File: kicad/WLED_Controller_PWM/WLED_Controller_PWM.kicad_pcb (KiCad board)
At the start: 2 copper layers, 72 x 50 mm, 59 parts, among them J1 USB_C_Receptacle_USB2.0, J5 Conn_01x05, J6 Conn_01x02, Q1 BC847, Q2 BC847, Q3 IRFL4105PBF, Q4 IRFL4105PBF, Q5 IRFL4105PBF, Q6 IRFL4105PBF, SW1 SW_RESET, SW2 SW_BOOT, SW3 SW_Push, U1 ESP32-WROOM-32, U2 CH340C, U3 NCP1117-3.3, U4 TSSP58P38, U5 L7805

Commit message: change mosfet
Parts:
- Q3, Q4, Q5, Q6: value IRFL4105PBF -> IRLL2705

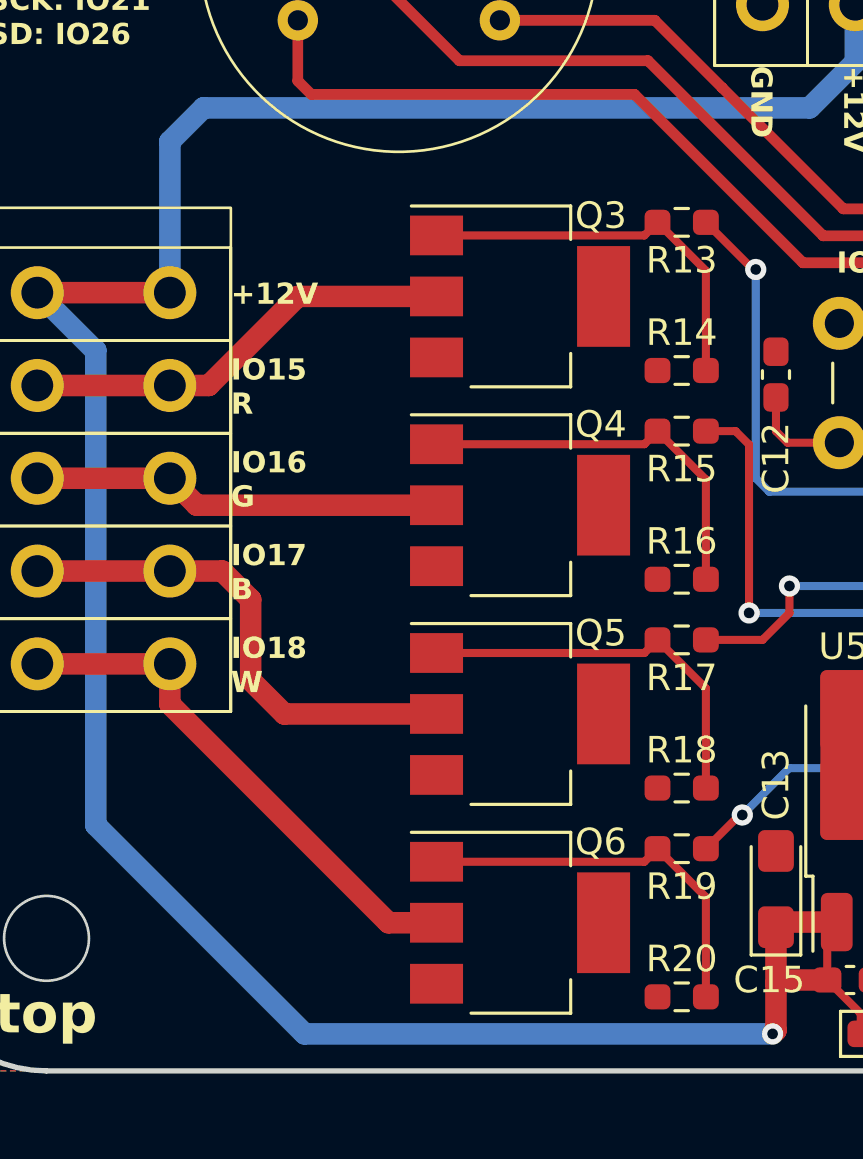
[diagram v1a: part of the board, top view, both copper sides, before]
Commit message: Do Not Place FETS
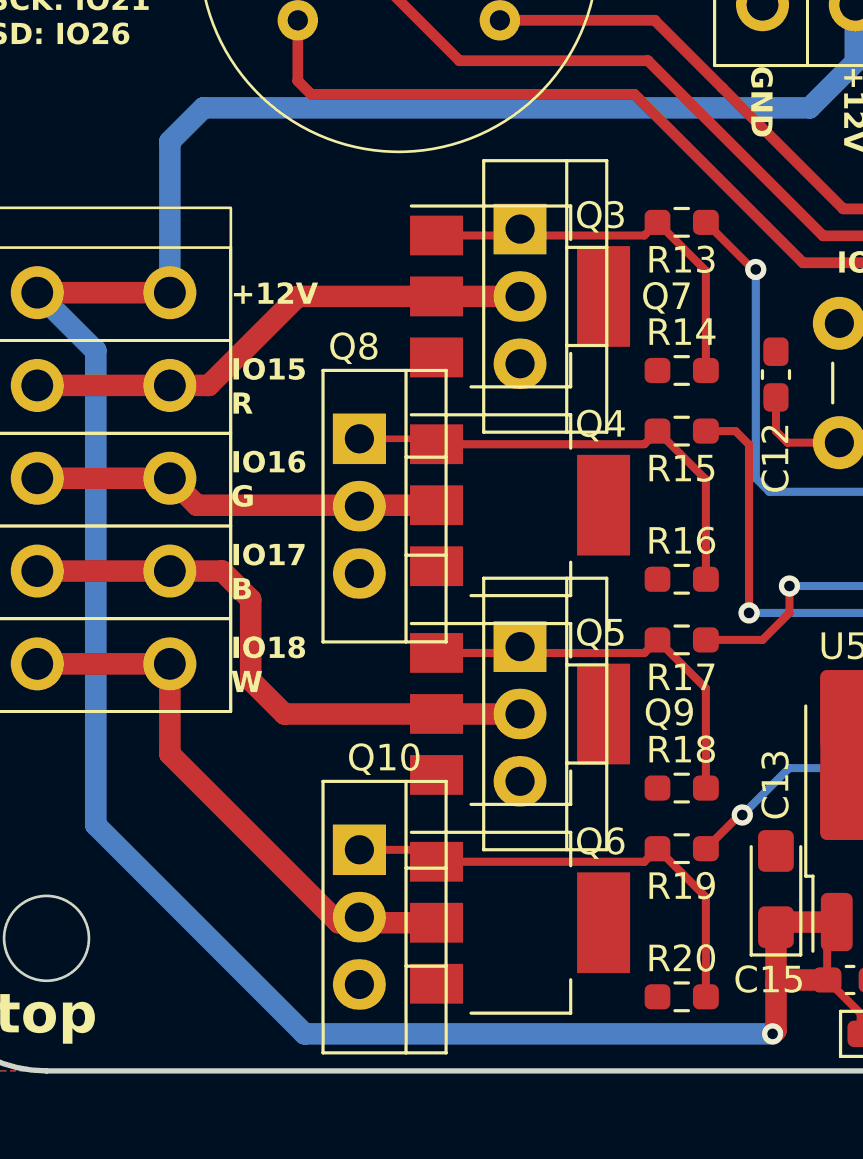
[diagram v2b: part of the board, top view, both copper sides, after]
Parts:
- added Q10: IRF540N, Package_TO_SOT_THT:TO-220-3_Vertical, F.Cu at (16.8, -8.34)
- added Q7: IRF540N, Package_TO_SOT_THT:TO-220-3_Vertical, F.Cu at (22.9, -31.8)
- added Q8: IRF540N, Package_TO_SOT_THT:TO-220-3_Vertical, F.Cu at (16.8, -23.8)
- added Q9: IRF540N, Package_TO_SOT_THT:TO-220-3_Vertical, F.Cu at (22.9, -16.0)
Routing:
- net Net-(Q5-G): track 14.9 -> 18.1 mm
- net Net-(J5-Pin_4): track 19.1 -> 22.2 mm
- net Net-(J5-Pin_2): track 16.4 -> 19.6 mm
- net Net-(Q10-G): track 14.9 -> 18.0 mm
- net Net-(Q4-G): track 14.9 -> 17.9 mm
- net Net-(J5-Pin_5): track 20.0 -> 21.1 mm

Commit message: Add new PCB-Layout
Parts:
- removed J5: Conn_01x05, GioN_Custom:WAGO_250-205_1x05_P3.50mm
- removed J6: Conn_01x02, GioN_Custom:WAGO_250-202_1x02_P3.50mm
- added J2: USB_C_Receptacle_USB2.0, GioN_Custom:USB_C, F.Cu at (50.0, -3.75)
- added J3: Conn_01x02, GioN_Custom:WAGO_250-202_1x02_P3.50mm, F.Cu at (8.60, -35.7)
- C12, C16, C8: value 100n -> 10u; footprint Capacitor_SMD:C_0603_1608Metric_Pad1.08x0.95mm_HandSolder -> Capacitor_Tantalum_SMD:CP_EIA-3216-18_Kemet-A_Pad1.58x1.35mm_HandSolder
- C14, C2, C3, C6: value 10u -> 100n; footprint Capacitor_Tantalum_SMD:CP_EIA-3216-18_Kemet-A_Pad1.58x1.35mm_HandSolder -> Capacitor_SMD:C_0603_1608Metric_Pad1.08x0.95mm_HandSolder
- C5: value 100n -> 10u; footprint Capacitor_SMD:C_0603_1608Metric_Pad1.08x0.95mm_HandSolder -> Capacitor_Tantalum_SMD:CP_EIA-3216-18_Kemet-A_Pad1.58x1.35mm_HandSolder; moved to F.Cu
- D1: value LED -> BAT60A; footprint LED_SMD:LED_0603_1608Metric_Pad1.05x0.95mm_HandSolder -> Diode_SMD:D_SOD-323_HandSoldering
- D3: value BAT60A -> INMP441; footprint Diode_SMD:D_SOD-323_HandSoldering -> GioN_Custom:INMP441_Module
- D5: value INMP441 -> BAT60A; footprint GioN_Custom:INMP441_Module -> Diode_SMD:D_SOD-323_HandSoldering
- D6: value BAT60A -> LED; footprint Diode_SMD:D_SOD-323_HandSoldering -> LED_SMD:LED_0603_1608Metric_Pad1.05x0.95mm_HandSolder
- J1: value USB_C_Receptacle_USB2.0 -> Conn_01x05; footprint GioN_Custom:USB_C -> GioN_Custom:WAGO_250-205_1x05_P3.50mm
- Q1, R4: moved to F.Cu
- Q10, Q8: value IRF540N -> IRLL2705; footprint Package_TO_SOT_THT:TO-220-3_Vertical -> Package_TO_SOT_SMD:SOT-223
- Q2: value BC847 -> IRF540N; footprint Package_TO_SOT_SMD:SOT-23 -> Package_TO_SOT_THT:TO-220-3_Vertical; moved to F.Cu
- Q4: value IRLL2705 -> IRF540N; footprint Package_TO_SOT_SMD:SOT-223 -> Package_TO_SOT_THT:TO-220-3_Vertical
- Q6: value IRLL2705 -> BC847; footprint Package_TO_SOT_SMD:SOT-223 -> Package_TO_SOT_SMD:SOT-23
- R1: value 1k -> 10k
- R10, R9: value 10k -> 5k1; moved to F.Cu
- R11: value 220R -> 10k
- R13, R15: value 100R -> 1k
- R14, R16: value 10k -> 100R
- R17, R19: value 100R -> 10k
- R18: value 10k -> 5k
- R2: value 1k -> 100R
- R20: value 10k -> 220R
- R3: value 5k1 -> 100R
- R5: value 5k1 -> 10k
- R6: value 5k -> 10k
- U1: value ESP32-WROOM-32 -> CH340C; footprint RF_Module:ESP32-WROOM-32 -> Package_SO:SOIC-16_3.9x9.9mm_P1.27mm
- U2: value CH340C -> TSSP58P38; footprint Package_SO:SOIC-16_3.9x9.9mm_P1.27mm -> Package_TO_SOT_THT:TO-92L_HandSolder; moved to F.Cu
- U3: value NCP1117-3.3 -> L7805; footprint Package_TO_SOT_SMD:SOT-223-3_TabPin2 -> Package_TO_SOT_SMD:TO-263-3_TabPin2
- U4: value TSSP58P38 -> ESP32-WROOM-32; footprint Package_TO_SOT_THT:TO-92L_HandSolder -> RF_Module:ESP32-WROOM-32
- U5: value L7805 -> NCP1117-3.3; footprint Package_TO_SOT_SMD:TO-252-3_TabPin2 -> Package_TO_SOT_SMD:SOT-223-3_TabPin2
- moved R17 63.3 mm to (87.7, -39.8), turned to -90 degrees
- moved C12 59.9 mm to (91.2, -38.5), turned to 0 degrees
- moved R16 59.8 mm to (88.5, -13.0), turned to 90 degrees
- moved R14 59.6 mm to (87.0, -13.0), turned to 90 degrees
- moved C15 54.8 mm to (69.4, -46.4)
- moved R18 51.1 mm to (80.0, -9.00)
- moved C16 50.7 mm to (72.8, -41.1), turned to 90 degrees
- moved R20 49.7 mm to (66.0, -36.0)
- moved D6 47.4 mm to (69.4, -36.0), turned to 180 degrees
- moved C14 46.4 mm to (66.0, -46.4), turned to 0 degrees
- moved C13 45.7 mm to (62.8, -41.1)
- moved Q6 44.6 mm to (66.9, -12.4)
- moved C4 44.3 mm to (88.4, -36.0)
- moved R19 43.7 mm to (70.2, -22.8), turned to 90 degrees
- moved U5 43.3 mm to (67.8, -41.2), turned to -90 degrees
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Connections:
- C12 pad 1: GND -> +3.3V
- C12 pad 2: Button0 -> GND
- C13 pad 1: +12V -> +5V
- C15 pad 1: +12V -> +3.3V
- C16 pad 1: +5V -> +3.3V
- C2 pad 1: +3.3V -> GND
- C2 pad 2: GND -> ESP_EN
- C3 pad 1: +3.3V -> GND
- C3 pad 2: GND -> ESP_IO0
- C5 pad 1: +3.3V -> +12V
- C6 pad 1: +5V -> +12V
- C8 pad 1: GND -> +5V
- C8 pad 2: ESP_EN -> GND
- C9 pad 2: ESP_IO0 -> Button0
- D1 pad 1: Net-(D1-K) -> +5V
- D1 pad 2: +3.3V -> Net-(D1-A)
- D3 pad 1: +5V -> GND
- D3 pad 2: Net-(D3-A) -> MIC_WS
- D4 pad 1: GND -> Net-(D4-K)
- D4 pad 2: Net-(D4-A) -> +3.3V
- D5 pad 1: GND -> +12V
- D5 pad 2: MIC_WS -> +5V
- D6 pad 1: +12V -> GND
- D6 pad 2: +5V -> Net-(D6-A)
- Q10 pad 2: Net-(J5-Pin_5) -> Net-(J1-Pin_5)
- Q2 pad 1: Net-(Q2-B) -> Net-(Q2-G)
- Q2 pad 2: ~{DTR} -> Net-(J1-Pin_2)
- Q2 pad 3: ESP_IO0 -> GND
- Q3 pad 1: Net-(Q3-G) -> Net-(Q2-G)
- Q3 pad 2: Net-(J5-Pin_2) -> Net-(J1-Pin_2)
- Q4 pad 2: Net-(J5-Pin_3) -> Net-(J1-Pin_3)
- Q5 pad 1: Net-(Q5-G) -> Net-(Q4-G)
- Q5 pad 2: Net-(J5-Pin_4) -> Net-(J1-Pin_3)
- Q6 pad 1: Net-(Q10-G) -> Net-(Q6-B)
- Q6 pad 2: Net-(J5-Pin_5) -> ~{DTR}
- Q6 pad 3: GND -> ESP_IO0
- Q7 pad 1: Net-(Q3-G) -> Net-(Q7-G)
- Q7 pad 2: Net-(J5-Pin_2) -> Net-(J1-Pin_4)
- Q8 pad 1: Net-(Q4-G) -> Net-(Q7-G)
- Q8 pad 2: Net-(J5-Pin_3) -> Net-(J1-Pin_4)
- Q9 pad 1: Net-(Q5-G) -> Net-(Q10-G)
- Q9 pad 2: Net-(J5-Pin_4) -> Net-(J1-Pin_5)
- R1 pad 1: TX -> ~{DTR}
- R1 pad 2: Net-(D1-K) -> Net-(Q1-B)
- R10 pad 1: ~{RTS} -> Net-(J2-CC1)
- R10 pad 2: Net-(Q2-B) -> GND
- R11 pad 1: +3.3V -> GND
- R11 pad 2: Net-(D4-A) -> Net-(Q7-G)
- R12 pad 1: +3.3V -> GND
- R12 pad 2: Button0 -> Net-(Q10-G)
- R13 pad 1: LED_R -> TX
- R13 pad 2: Net-(Q3-G) -> Net-(D2-K)
- R14 pad 1: GND -> TX
- R14 pad 2: Net-(Q3-G) -> ESP_RX
- R15 pad 1: LED_G -> RX
- R15 pad 2: Net-(Q4-G) -> Net-(D4-K)
- R16 pad 1: GND -> RX
- R16 pad 2: Net-(Q4-G) -> ESP_TX
- R17 pad 1: LED_B -> +3.3V
- R17 pad 2: Net-(Q5-G) -> ESP_EN
- R18 pad 1: GND -> +3.3V
- R18 pad 2: Net-(Q5-G) -> ESP_IO0
- R19 pad 1: LED_W -> +3.3V
- R19 pad 2: Net-(Q10-G) -> Button0
- R2 pad 1: RX -> LED_R
- R2 pad 2: Net-(D2-K) -> Net-(Q2-G)
- R20 pad 1: GND -> +3.3V
- R20 pad 2: Net-(Q10-G) -> Net-(D6-A)
- R3 pad 1: Net-(J1-CC2) -> LED_G
- R3 pad 2: GND -> Net-(Q4-G)
- R4 pad 1: +3.3V -> GND
- R4 pad 2: ESP_EN -> Net-(Q2-G)
- R5 pad 1: Net-(J1-CC1) -> GND
- R5 pad 2: GND -> Net-(Q4-G)
- R6 pad 1: +3.3V -> ~{RTS}
- R6 pad 2: ESP_IO0 -> Net-(Q6-B)
- R7 pad 1: TX -> LED_B
- R7 pad 2: ESP_RX -> Net-(Q7-G)
- R8 pad 1: RX -> LED_W
- R8 pad 2: ESP_TX -> Net-(Q10-G)
- R9 pad 1: ~{DTR} -> Net-(J2-CC2)
- R9 pad 2: Net-(Q1-B) -> GND
- U1 pad 10: IO25 -> unconnected-(U1-~{DSR}-Pad10)
- U1 pad 11: MIC_SD -> unconnected-(U1-~{RI}-Pad11)
- U1 pad 12: SENSE0 -> unconnected-(U1-~{DCD}-Pad12)
- U1 pad 13: IO14 -> ~{DTR}
- U1 pad 14: IO12 -> ~{RTS}
- U1 pad 15: GND -> unconnected-(U1-R232-Pad15)
- U1 pad 16: IO13 -> +3.3V
- U1 pad 2: +3.3V -> TX
- U1 pad 3: ESP_EN -> RX
- U1 pad 4: unconnected-(U1-SENSOR_VP-Pad4) -> +3.3V
- U1 pad 5: unconnected-(U1-SENSOR_VN-Pad5) -> D+
- U1 pad 6: IO34 -> D-
- U1 pad 7: IO35 -> unconnected-(U1-NC-Pad7)
- U1 pad 8: IO32 -> unconnected-(U1-NC-Pad8)
- U1 pad 9: IO33 -> unconnected-(U1-~{CTS}-Pad9)
- U2 pad 1: GND -> SENSE0
- U2 pad 2: TX -> GND
- U2 pad 3: RX -> +3.3V
- U3 pad 1: GND -> +12V
- U3 pad 2: +3.3V -> GND
- U4 pad 1: SENSE0 -> GND
- U4 pad 2: GND -> +3.3V
- U4 pad 3: +3.3V -> ESP_EN
- U5 pad 1: +12V -> GND
- U5 pad 2: GND -> +3.3V
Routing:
- net +12V: track 108.1 -> 52.7 mm
- net TX: track 8.27 -> 51.8 mm, vias 1 -> 4
- net RX: track 12.1 -> 55.3 mm, vias 1 -> 4
- net Net-(J1-Pin_5): track 0.00 -> 36.2 mm, vias 0 -> 1
- net Net-(J1-Pin_4): track 0.00 -> 32.0 mm, vias 0 -> 1
- net Net-(J1-Pin_2): track 0.00 -> 29.2 mm, vias 0 -> 1
- net Net-(J1-Pin_3): track 0.00 -> 28.0 mm, vias 0 -> 1
- net LED_R: track 26.7 -> 50.2 mm
- net Net-(J5-Pin_4): track 22.2 -> 0.00 mm
- net Net-(Q2-G): track 0.00 -> 22.0 mm
- net Net-(Q7-G): track 0.00 -> 22.0 mm
- net SENSE0: track 15.9 -> 37.1 mm, vias 0 -> 1
- net Net-(J5-Pin_5): track 21.1 -> 0.00 mm
- net LED_B: track 25.0 -> 45.6 mm
- net LED_G: track 28.5 -> 48.4 mm
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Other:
- board size 72 x 50 mm -> 100 x 50 mm
- board text added: "+"
- board text added: "-"
- board text added: "B"
- board text added: "G"
- board text added: "IR - IO27"
- board text added: "MIC_WS - IO05 MIC_SCK - IO21 MIC_SD - IO26"
- board text added: "R"
- board text added: "R - IO15 G - IO16 B - IO17 W - IO18"
- board text added: "W"
- board text added: "WLED-Controller (PWM) Ver.1 Rev.0 02/25 Gioulekas Nikos"
- board text removed: "+12V"
- board text removed: "BOOT"
- board text removed: "GND"
- board text removed: "IO15 R"
- board text removed: "IO16 G"
- board text removed: "IO17 B"
- board text removed: "IO18 W"
- board text removed: "IO19 BTN0"
- board text removed: "IO27 REM"
- board text removed: "RST"
- board text removed: "WLED Controller PWM V1 R1 05/2024 Gioulekas Nikos"
- board text removed: "WS: IO05 SCK: IO21 SD: IO26"
- board text removed: "bot"
- board text removed: "top"
